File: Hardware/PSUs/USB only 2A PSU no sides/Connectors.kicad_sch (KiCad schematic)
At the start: 11 parts, among them J10 G-Switch-GT-USB-7025, J11 1.27mm 4 pin socket, J3 Keystone 3579, J5 Keystone 3569, J7 Keystone 3579, J9 Keystone 3569

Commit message: Finished schematic, started arrangement
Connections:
- net GND: no longer J10.GND
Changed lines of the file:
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@@
 		(pin "B5"
-		)
-		(pin "GND"
 		)
 		(instances
@@
 	)
 	(symbol
+		(lib_name "R_Small_1")
 		(lib_id "Device:R_Small")
 		(at 125.73 62.23 180)

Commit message: Moved current sense to PSU schematic
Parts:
- R19, R33: footprint Resistor_SMD:R_0402_1005Metric -> Resistor_SMD:R_0805_2012Metric
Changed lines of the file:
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@@
 			)
 		)
-		(property "Footprint" "Resistor_SMD:R_0402_1005Metric"
+		(property "Footprint" "Resistor_SMD:R_0805_2012Metric"
 			(at 119.38 64.77 0)
 			(effects
@@
 			)
 		)
-		(property "Footprint" "Resistor_SMD:R_0402_1005Metric"
+		(property "Footprint" "Resistor_SMD:R_0805_2012Metric"
 			(at 125.73 62.23 0)
 			(effects

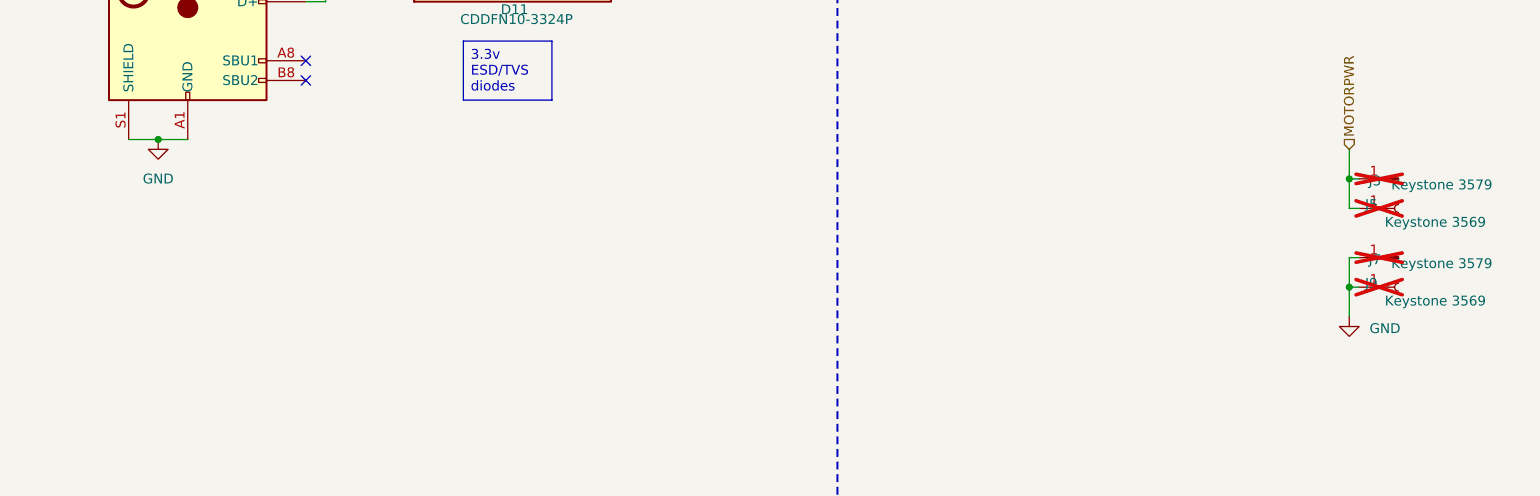
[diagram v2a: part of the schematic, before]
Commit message: Added USB bus and finished preliminary routing
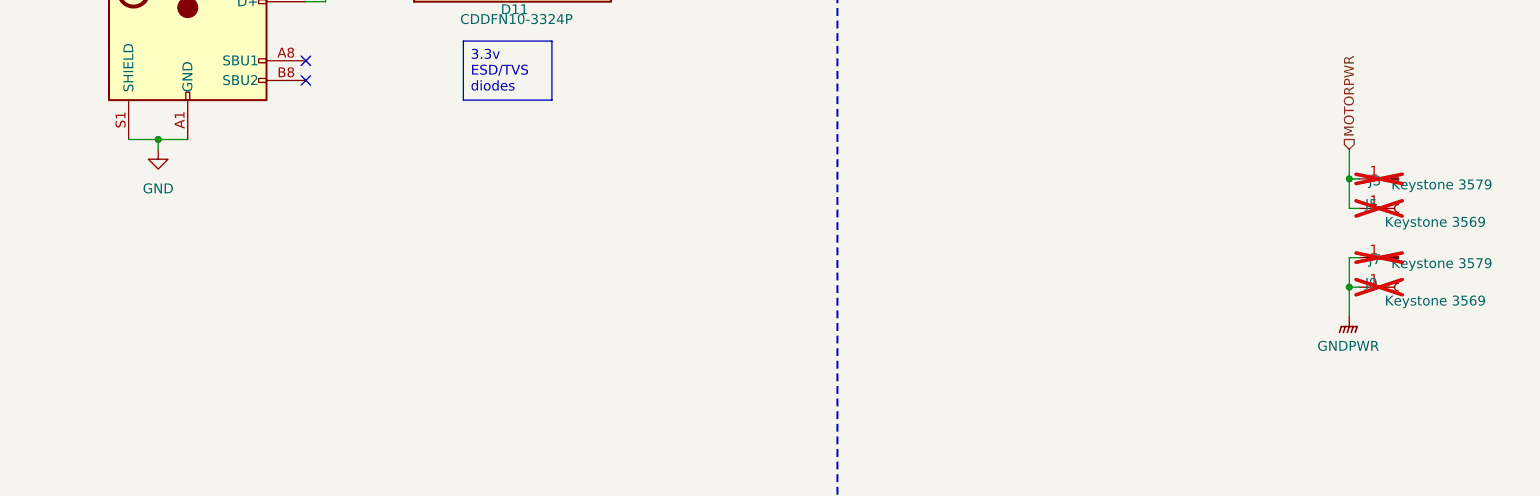
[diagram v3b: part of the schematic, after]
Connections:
- net GND: no longer J7.1 (Pin_1), J9.1 (Pin_1)
- new net GNDPWR: J7.1 (Pin_1), J9.1 (Pin_1)
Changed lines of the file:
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@@
+	(wire
+		(pts
+			(xy 48.26 91.44) (xy 48.26 90.17)
+		)
+		(stroke
+			(width 0)
+			(type default)
+		)
+	)
 	(wire
 		(pts
@@
 	)
 	(symbol
+		(lib_id "power:GNDPWR")
+		(at 201.93 113.03 0)
+		(unit 1)
+		(exclude_from_sim no)
+		(in_bom yes)
+		(on_board yes)
+		(dnp no)
+		(fields_autoplaced yes)
+		(property "Reference" "#PWR08"
+			(at 201.93 118.11 0)
+			(effects
+				(font
+					(size 1.27 1.27)
+				)
+				(hide yes)
+			)
+		)
+		(property "Value" "GNDPWR"
+			(at 201.803 116.84 0)
+			(effects
+				(font
+					(size 1.27 1.27)
+				)
+			)
+		)
+		(property "Footprint" ""
+			(at 201.93 114.3 0)
+			(effects
+				(font
+					(size 1.27 1.27)
+				)
+				(hide yes)
+			)
+		)
+		(property "Datasheet" ""
+			(at 201.93 114.3 0)
+			(effects
+				(font
+					(size 1.27 1.27)
+				)
+				(hide yes)
+			)
+		)
+		(property "Description" "Power symbol creates a global label with name \"GNDPWR\" , global ground"
+			(at 201.93 113.03 0)
+			(effects
+				(font
+					(size 1.27 1.27)
+				)
+				(hide yes)
+			)
+		)
+		(pin "1"
+		)
+		(instances
+			(project "USB only 2A PSU no sides"
+				(path "/eb3f183d-8bb1-43a5-a363-092ed67891e3/3a3003bc-8e40-4cd7-b859-421f37e4b48c"
+					(reference "#PWR08")
+					(unit 1)
+				)
+			)
+		)
+	)
+	(symbol
 		(lib_id "power:PWR_FLAG")
 		(at 76.2 44.45 0)
@@
 	)
 	(symbol
-		(lib_id "power:GND")
-		(at 201.93 113.03 0)
-		(unit 1)
-		(exclude_from_sim no)
-		(in_bom yes)
-		(on_board yes)
-		(dnp no)
-		(property "Reference" "#PWR08"
-			(at 201.93 119.38 0)
-			(effects
-				(font
-					(size 1.27 1.27)
-				)
-				(hide yes)
-			)
-		)
-		(property "Value" "GND"
-			(at 208.534 114.554 0)
-			(effects
-				(font
-					(size 1.27 1.27)
-				)
-				(justify right)
-			)
-		)
-		(property "Footprint" ""
-			(at 201.93 113.03 0)
-			(effects
-				(font
-					(size 1.27 1.27)
-				)
-				(hide yes)
-			)
-		)
-		(property "Datasheet" ""
-			(at 201.93 113.03 0)
-			(effects
-				(font
-					(size 1.27 1.27)
-				)
-				(hide yes)
-			)
-		)
-		(property "Description" "Power symbol creates a global label with name \"GND\" , ground"
-			(at 201.93 113.03 0)
-			(effects
-				(font
-					(size 1.27 1.27)
-				)
-				(hide yes)
-			)
-		)
-		(pin "1"
-		)
-		(instances
-			(project "2s 40A PSU and charger"
-				(path "/eb3f183d-8bb1-43a5-a363-092ed67891e3/3a3003bc-8e40-4cd7-b859-421f37e4b48c"
-					(reference "#PWR08")
-					(unit 1)
-				)
-			)
-		)
-	)
-	(symbol
 		(lib_id "Device:R_Small")
 		(at 119.38 64.77 180)
@@
 	(symbol
 		(lib_id "power:GND")
-		(at 48.26 90.17 0)
+		(at 48.26 91.44 0)
 		(unit 1)
 		(exclude_from_sim no)
@@
 		(fields_autoplaced yes)
 		(property "Reference" "#PWR02"
+			(at 48.26 97.79 0)
+			(effects
+				(font
+					(size 1.27 1.27)
+				)
+				(hide yes)
+			)
+		)
+		(property "Value" "GND"
 			(at 48.26 96.52 0)
 			(effects
@@
 					(size 1.27 1.27)
 				)
-				(hide yes)
-			)
-		)
-		(property "Value" "GND"
-			(at 48.26 95.25 0)
-			(effects
-				(font
-					(size 1.27 1.27)
-				)
 			)
 		)
 		(property "Footprint" ""
-			(at 48.26 90.17 0)
+			(at 48.26 91.44 0)
 			(effects
 				(font
@@
 		)
 		(property "Datasheet" ""
-			(at 48.26 90.17 0)
+			(at 48.26 91.44 0)
 			(effects
 				(font
@@
 		)
 		(property "Description" "Power symbol creates a global label with name \"GND\" , ground"
-			(at 48.26 90.17 0)
-			(effects
-				(font
+			(at 48.26 91.44 0)
+			(effects
+				(font

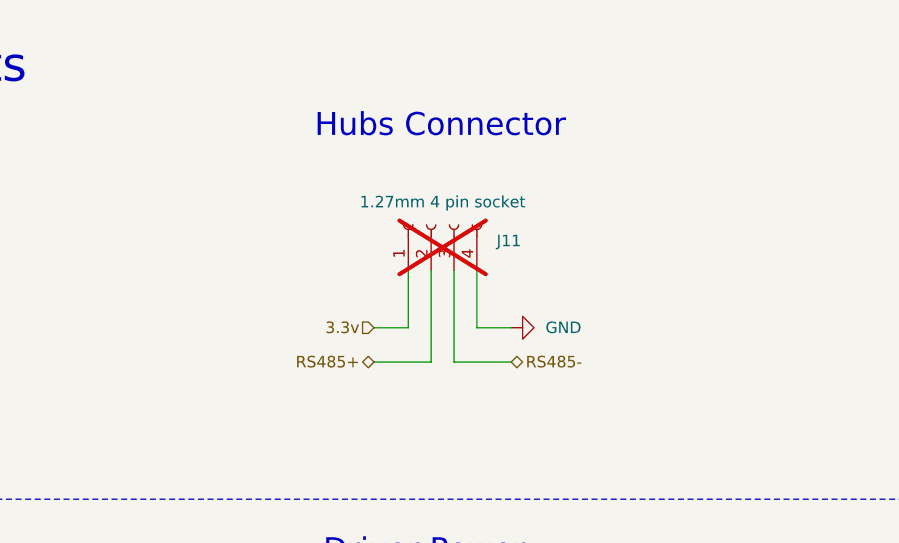
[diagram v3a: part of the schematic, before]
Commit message: revised ground circuit
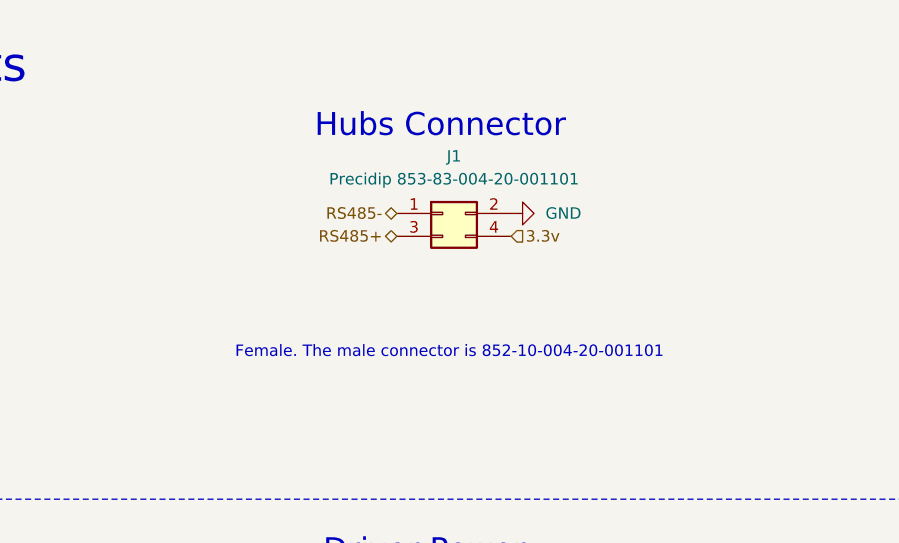
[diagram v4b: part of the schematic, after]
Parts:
- removed J11: 1.27mm 4 pin socket, Connector_PinSocket_1.27mm:PinSocket_1x04_P1.27mm_Vertical, symbol Connector:Conn_01x04_Socket
- added J1: Precidip 853-83-004-20-001101, Connector_PinHeader_1.27mm:PinHeader_2x02_P1.27mm_Horizontal, symbol Connector_Generic:Conn_02x02_Odd_Even
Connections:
- net 3.3v: now also J1.4 (Pin_4)
- net GND: now also J1.2 (Pin_2)
- net RS485+: now also J1.3 (Pin_3)
- net RS485-: now also J1.1 (Pin_1)
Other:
- note added: "Female. The male connector is 852-10-004-20-001101"
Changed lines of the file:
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@@
 		(comment 1 "Licensed under CERN-OHL-S")
+	)
+	(text "Female. The male connector is 852-10-004-20-001101"
+		(exclude_from_sim no)
+		(at 206.502 48.514 0)
+		(effects
+			(font
+				(size 1.27 1.27)
+			)
+		)
 	)
 	(text "Outputs"
@@
 	(wire
 		(pts
-			(xy 207.01 39.37) (xy 207.01 49.53)
-		)
-		(stroke
-			(width 0)
-			(type default)
-		)
-	)
-	(wire
-		(pts
 			(xy 201.93 95.25) (xy 203.2 95.25)
 		)
@@
 	(wire
 		(pts
-			(xy 198.12 45.72) (xy 201.93 45.72)
-		)
-		(stroke
-			(width 0)
-			(type default)
-		)
-	)
-	(wire
-		(pts
-			(xy 209.55 39.37) (xy 209.55 45.72)
-		)
-		(stroke
-			(width 0)
-			(type default)
-		)
-	)
-	(wire
-		(pts
 			(xy 76.2 69.85) (xy 111.76 69.85)
 		)
@@
 	(wire
 		(pts
-			(xy 207.01 49.53) (xy 213.36 49.53)
-		)
-		(stroke
-			(width 0)
-			(type default)
-		)
-	)
-	(wire
-		(pts
 			(xy 111.76 64.77) (xy 121.92 64.77)
-		)
-		(stroke
-			(width 0)
-			(type default)
-		)
-	)
-	(wire
-		(pts
-			(xy 201.93 39.37) (xy 201.93 45.72)
 		)
 		(stroke
@@
 	(wire
 		(pts
-			(xy 204.47 39.37) (xy 204.47 49.53)
-		)
-		(stroke
-			(width 0)
-			(type default)
-		)
-	)
-	(wire
-		(pts
 			(xy 69.85 59.69) (xy 76.2 59.69)
 		)
@@
 	(wire
 		(pts
-			(xy 198.12 49.53) (xy 204.47 49.53)
-		)
-		(stroke
-			(width 0)
-			(type default)
-		)
-	)
-	(wire
-		(pts
 			(xy 76.2 44.45) (xy 76.2 52.07)
 		)
@@
 		(pts
 			(xy 76.2 52.07) (xy 67.31 52.07)
-		)
-		(stroke
-			(width 0)
-			(type default)
-		)
-	)
-	(wire
-		(pts
-			(xy 209.55 45.72) (xy 213.36 45.72)
 		)
 		(stroke
@@
 	(hierarchical_label "RS485+"
 		(shape bidirectional)
-		(at 198.12 49.53 180)
+		(at 200.66 35.56 180)
 		(effects
 			(font
@@
 	(hierarchical_label "3.3v"
 		(shape input)
-		(at 198.12 45.72 180)
+		(at 213.36 35.56 0)
 		(fields_autoplaced yes)
 		(effects
@@
 				(size 1.27 1.27)
 			)
-			(justify right)
+			(justify left)
 		)
 		(property "Netclass" "Charge Current"
-			(at 198.12 46.99 0)
+			(at 213.36 36.83 0)
 			(effects
 				(font
@@
 					(italic yes)
 				)
-				(justify right)
+				(justify left)
 			)
 		)
@@
 	(hierarchical_label "RS485-"
 		(shape bidirectional)
-		(at 213.36 49.53 0)
+		(at 200.66 33.02 180)
 		(effects
 			(font
 				(size 1.27 1.27)
 			)
-			(justify left)
+			(justify right)
 		)
 	)
@@
 	(symbol
 		(lib_id "power:GND")
-		(at 213.36 45.72 90)
+		(at 213.36 33.02 90)
 		(unit 1)
 		(exclude_from_sim no)
@@
 		(fields_autoplaced yes)
 		(property "Reference" "#PWR028"
-			(at 219.71 45.72 0)
+			(at 219.71 33.02 0)
 			(effects
 				(font
@@
 		)
 		(property "Value" "GND"
-			(at 217.17 45.7199 90)
+			(at 217.17 33.0199 90)
 			(effects
 				(font
@@
 		)
 		(property "Footprint" ""
-			(at 213.36 45.72 0)
+			(at 213.36 33.02 0)
 			(effects
 				(font
@@
 		)
 		(property "Datasheet" ""
-			(at 213.36 45.72 0)
+			(at 213.36 33.02 0)
 			(effects
 				(font
@@
 		)
 		(property "Description" "Power symbol creates a global label with name \"GND\" , ground"
-			(at 213.36 45.72 0)
+			(at 213.36 33.02 0)
 			(effects
 				(font
@@
 				(path "/eb3f183d-8bb1-43a5-a363-092ed67891e3/3a3003bc-8e40-4cd7-b859-421f37e4b48c"
 					(reference "C7")
+					(unit 1)
+				)
+			)
+		)
+	)
+	(symbol
+		(lib_id "Connector_Generic:Conn_02x02_Odd_Even")
+		(at 205.74 33.02 0)
+		(unit 1)
+		(exclude_from_sim no)
+		(in_bom yes)
+		(on_board yes)
+		(dnp no)
+		(fields_autoplaced yes)
+		(property "Reference" "J1"
+			(at 207.01 26.67 0)
+			(effects
+				(font
+					(size 1.27 1.27)
+				)
+			)
+		)
+		(property "Value" "Precidip 853-83-004-20-001101"
+			(at 207.01 29.21 0)
+			(effects
+				(font
+					(size 1.27 1.27)
+				)
+			)
+		)
+		(property "Footprint" "Connector_PinHeader_1.27mm:PinHeader_2x02_P1.27mm_Horizontal"
+			(at 205.74 33.02 0)
+			(effects
+				(font
+					(size 1.27 1.27)
+				)
+				(hide yes)
+			)
+		)
+		(property "Datasheet" "~"
+			(at 205.74 33.02 0)
+			(effects
+				(font
+					(size 1.27 1.27)
+				)
+				(hide yes)
+			)
+		)
+		(property "Description" "Generic connector, double row, 02x02, odd/even pin numbering scheme (row 1 odd numbers, row 2 even numbers), script generated (kicad-library-utils/schlib/autogen/connector/)"
+			(at 205.74 33.02 0)
+			(effects
+				(font
+					(size 1.27 1.27)
+				)
+				(hide yes)
+			)
+		)
+		(pin "3"
+		)
+		(pin "2"
+		)
+		(pin "4"
+		)
+		(pin "1"
+		)
+		(instances
+			(project ""
+				(path "/eb3f183d-8bb1-43a5-a363-092ed67891e3/3a3003bc-8e40-4cd7-b859-421f37e4b48c"
+					(reference "J1")
 					(unit 1)
 				)
@@
 					(unit 1)
 				)
-			)
-		)
-	)
-	(symbol
-		(lib_id "Connector:Conn_01x04_Socket")
-		(at 204.47 34.29 90)
-		(unit 1)
-		(exclude_from_sim no)
-		(in_bom yes)
-		(on_board yes)
-		(dnp yes)
-		(property "Reference" "J11"
-			(at 213.106 36.068 90)
-			(effects
-				(font
-					(size 1.27 1.27)
-				)
-			)
-		)
-		(property "Value" "1.27mm 4 pin socket"
-			(at 205.74 31.75 90)
-			(effects
-				(font
-					(size 1.27 1.27)
-				)
-			)
-		)
-		(property "Footprint" "Connector_PinSocket_1.27mm:PinSocket_1x04_P1.27mm_Vertical"
-			(at 204.47 34.29 0)
-			(effects
-				(font
-					(size 1.27 1.27)
-				)
-				(hide yes)
-			)
-		)
-		(property "Datasheet" "~"
-			(at 204.47 34.29 0)
-			(effects
-				(font
-					(size 1.27 1.27)
-				)
-				(hide yes)
-			)
-		)
-		(property "Description" "Generic connector, single row, 01x04, script generated"
-			(at 204.47 34.29 0)
-			(effects
-				(font
-					(size 1.27 1.27)
-				)
-				(hide yes)
-			)
-		)
-		(pin "3"
-		)
-		(pin "4"
-		)
-		(pin "2"
-		)
-		(pin "1"
-		)
-		(instances
-			(project "2s 40A PSU and charger"
-				(path "/eb3f183d-8bb1-43a5-a363-092ed67891e3/3a3003bc-8e40-4cd7-b859-421f37e4b48c"
-					(reference "J11")
-					(unit 1)
-				)
-			)
-			(project "Connectors"
-				(path "/ef905b65-82b7-484f-997c-0c6089b83b28"
-					(reference "J?")
-					(unit 1)
-				)

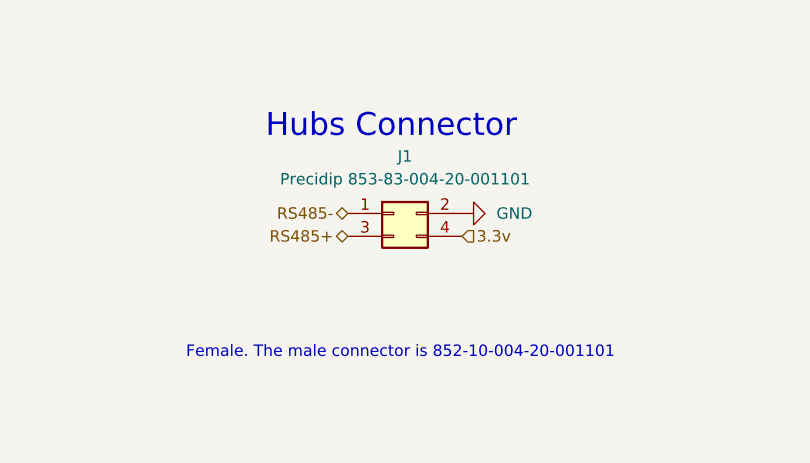
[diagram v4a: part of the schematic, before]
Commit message: Updated connector part ID, added production files
I messed on on a single number 83 vs 87. The difference is in the plating, and 83 is not available anywhere
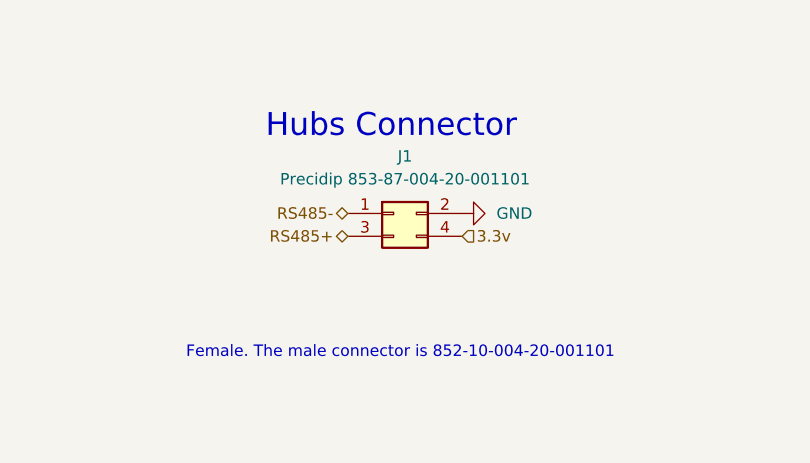
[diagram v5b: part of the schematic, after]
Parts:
- J1: value Precidip 853-83-004-20-001101 -> Precidip 853-87-004-20-001101
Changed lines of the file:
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@@
 			)
 		)
-		(property "Value" "Precidip 853-83-004-20-001101"
+		(property "Value" "Precidip 853-87-004-20-001101"
 			(at 207.01 29.21 0)
 			(effects
